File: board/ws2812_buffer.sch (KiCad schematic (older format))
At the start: 5 parts

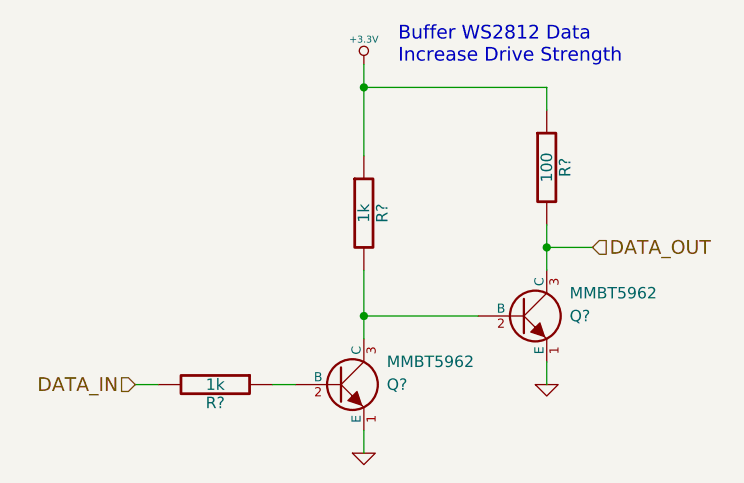
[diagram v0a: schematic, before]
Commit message: Reiner Documentation, Industrial GPIO, Driver Fix
I added documentation for the meaning of Reiner's board pins. I have
finished implemented the industrial inputs on the schematic and partial
industrial outputs. I have added some capacitors to the motor drivers.
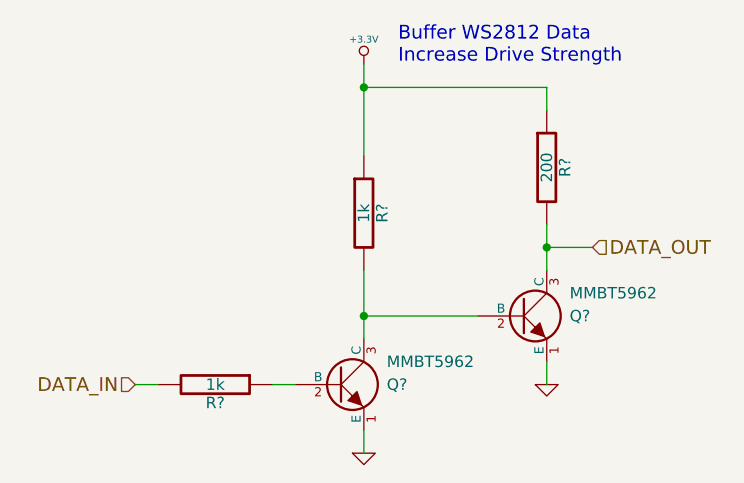
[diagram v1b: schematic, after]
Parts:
- R?: value 100 -> 200
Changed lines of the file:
@@
 $Descr USLetter 11000 8500
 encoding utf-8
-Sheet 8 10
+Sheet 8 26
 Title "WS2812 Buffered Output"
 Date ""
@@
 P 6150 4000
 F 0 "R?" V 6230 4000 50  0000 C CNN
-F 1 "100" V 6150 4000 50  0000 C CNN
+F 1 "200" V 6150 4000 50  0000 C CNN
 F 2 "" H 6150 4000 60  0000 C CNN
 F 3 "" H 6150 4000 60  0000 C CNN

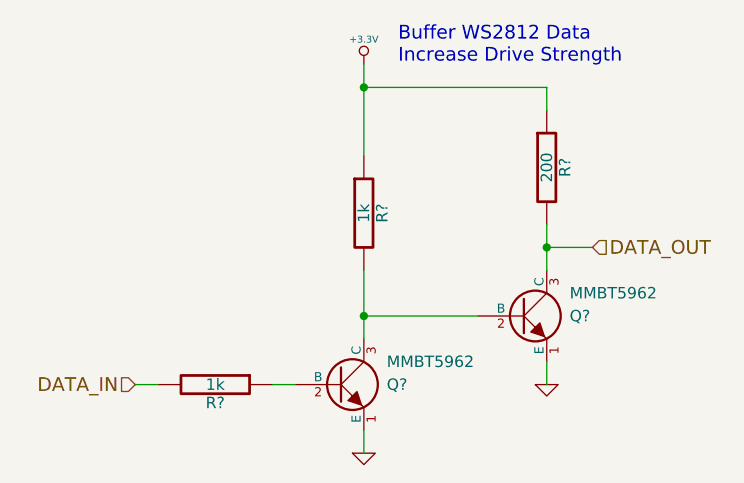
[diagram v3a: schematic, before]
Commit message: Fixed ERC Errors. Annotated all components.
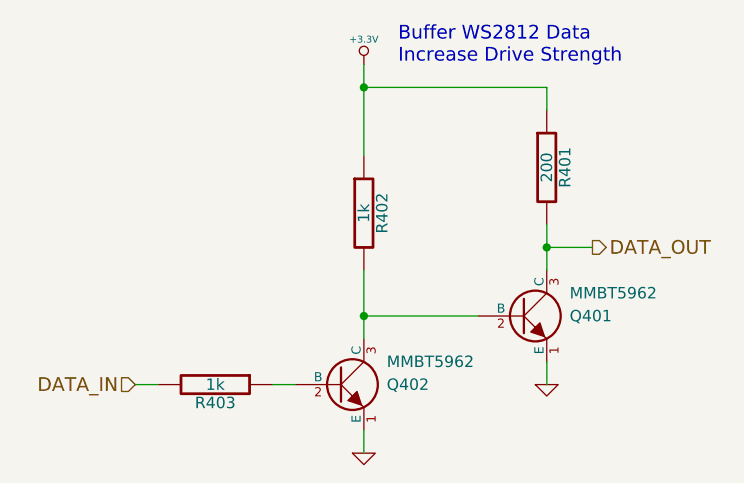
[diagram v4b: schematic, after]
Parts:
- gave numbers to parts that had none: 5
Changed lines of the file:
@@
 $EndDescr
 $Comp
-L NPN Q?
+L NPN Q402
 U 1 1 52EEEE15
 P 5250 4950
-F 0 "Q?" H 5450 4950 50  0000 L CNN
+AR Path="/52EF032B/52EEEE15" Ref="Q402"  Part="1"
+AR Path="/52EF6BF1/52EEEE15" Ref="Q502"  Part="1"
+F 0 "Q402" H 5450 4950 50  0000 L CNN
 F 1 "MMBT5962" H 5450 5050 50  0000 L CNN
 F 2 "" H 5250 4950 60  0000 C CNN
@@
 $EndComp
 $Comp
-L R R?
+L R R403
 U 1 1 52EEEE2E
 P 4700 4950
-F 0 "R?" V 4780 4950 50  0000 C CNN
+AR Path="/52EF032B/52EEEE2E" Ref="R403"  Part="1"
+AR Path="/52EF6BF1/52EEEE2E" Ref="R503"  Part="1"
+F 0 "R403" V 4780 4950 50  0000 C CNN
 F 1 "1k" V 4700 4950 50  0000 C CNN
 F 2 "" H 4700 4950 60  0000 C CNN
@@
 $EndComp
 $Comp
-L GND #PWR?
+L GND #PWR0124
 U 1 1 52EEEE49
 P 5350 5250
-F 0 "#PWR?" H 5350 5250 30  0001 C CNN
+AR Path="/52EF032B/52EEEE49" Ref="#PWR0124"  Part="1"
+AR Path="/52EF6BF1/52EEEE49" Ref="#PWR0127"  Part="1"
+F 0 "#PWR0127" H 5350 5250 30  0001 C CNN
 F 1 "GND" H 5350 5180 30  0001 C CNN
 F 2 "" H 5350 5250 60  0000 C CNN
@@
 $EndComp
 $Comp
-L R R?
+L R R402
 U 1 1 52EEEE6D
 P 5350 4200
-F 0 "R?" V 5430 4200 50  0000 C CNN
+AR Path="/52EF032B/52EEEE6D" Ref="R402"  Part="1"
+AR Path="/52EF6BF1/52EEEE6D" Ref="R502"  Part="1"
+F 0 "R402" V 5430 4200 50  0000 C CNN
 F 1 "1k" V 5350 4200 50  0000 C CNN
 F 2 "" H 5350 4200 60  0000 C CNN
@@
 $EndComp
 $Comp
-L +3.3V #PWR?
+L +3.3V #PWR0125
 U 1 1 52EEEE7E
 P 5350 3550
-F 0 "#PWR?" H 5350 3510 30  0001 C CNN
+AR Path="/52EF032B/52EEEE7E" Ref="#PWR0125"  Part="1"
+AR Path="/52EF6BF1/52EEEE7E" Ref="#PWR0128"  Part="1"
+F 0 "#PWR0128" H 5350 3510 30  0001 C CNN
 F 1 "+3.3V" H 5350 3660 30  0000 C CNN
 F 2 "" H 5350 3550 60  0000 C CNN
@@
 $EndComp
 $Comp
-L NPN Q?
+L NPN Q401
 U 1 1 52EEEE90
 P 6050 4650
-F 0 "Q?" H 6250 4650 50  0000 L CNN
+AR Path="/52EF032B/52EEEE90" Ref="Q401"  Part="1"
+AR Path="/52EF6BF1/52EEEE90" Ref="Q501"  Part="1"
+F 0 "Q401" H 6250 4650 50  0000 L CNN
 F 1 "MMBT5962" H 6250 4750 50  0000 L CNN
 F 2 "" H 6050 4650 60  0000 C CNN
@@
 $EndComp
 $Comp
-L GND #PWR?
+L GND #PWR0126
 U 1 1 52EEEE97
 P 6150 4950
-F 0 "#PWR?" H 6150 4950 30  0001 C CNN
+AR Path="/52EF032B/52EEEE97" Ref="#PWR0126"  Part="1"
+AR Path="/52EF6BF1/52EEEE97" Ref="#PWR0129"  Part="1"
+F 0 "#PWR0129" H 6150 4950 30  0001 C CNN
 F 1 "GND" H 6150 4880 30  0001 C CNN
 F 2 "" H 6150 4950 60  0000 C CNN
@@
 $EndComp
 $Comp
-L R R?
+L R R401
 U 1 1 52EEEE9E
 P 6150 4000
-F 0 "R?" V 6230 4000 50  0000 C CNN
+AR Path="/52EF032B/52EEEE9E" Ref="R401"  Part="1"
+AR Path="/52EF6BF1/52EEEE9E" Ref="R501"  Part="1"
+F 0 "R401" V 6230 4000 50  0000 C CNN
 F 1 "200" V 6150 4000 50  0000 C CNN
 F 2 "" H 6150 4000 60  0000 C CNN
@@
 Text HLabel 4350 4950 0    60   Input ~ 0
 DATA_IN
-Text HLabel 6350 4350 2    60   Input ~ 0
+Text HLabel 6350 4350 2    60   Output ~ 0
 DATA_OUT
 Wire Wire Line

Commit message: Selected Part Numbers for all Components
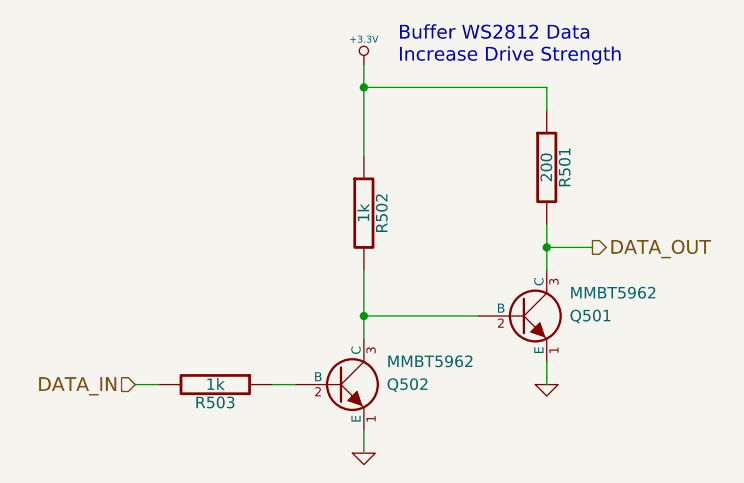
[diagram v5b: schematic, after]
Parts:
- Q401, Q402: Part Number (none) -> MMBT5962
- R401: Part Number (none) -> RC1608J201CS
- R402, R403: Part Number (none) -> RC1608J102CS
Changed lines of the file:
@@
 AR Path="/52EF032B/52EEEE15" Ref="Q402"  Part="1"
 AR Path="/52EF6BF1/52EEEE15" Ref="Q502"  Part="1"
-F 0 "Q402" H 5450 4950 50  0000 L CNN
+F 0 "Q502" H 5450 4950 50  0000 L CNN
 F 1 "MMBT5962" H 5450 5050 50  0000 L CNN
 F 2 "" H 5250 4950 60  0000 C CNN
 F 3 "" H 5250 4950 60  0000 C CNN
+F 4 "MMBT5962" H 5250 4950 60  0001 C CNN "Part Number"
 	1    5250 4950
 	1    0    0    -1
@@
 AR Path="/52EF032B/52EEEE2E" Ref="R403"  Part="1"
 AR Path="/52EF6BF1/52EEEE2E" Ref="R503"  Part="1"
-F 0 "R403" V 4780 4950 50  0000 C CNN
+F 0 "R503" V 4780 4950 50  0000 C CNN
 F 1 "1k" V 4700 4950 50  0000 C CNN
 F 2 "" H 4700 4950 60  0000 C CNN
 F 3 "" H 4700 4950 60  0000 C CNN
+F 4 "RC1608J102CS" V 4700 4950 60  0001 C CNN "Part Number"
 	1    4700 4950
 	0    1    1    0
 $EndComp
 $Comp
-L GND #PWR0124
+L GND #PWR0129
 U 1 1 52EEEE49
 P 5350 5250
-AR Path="/52EF032B/52EEEE49" Ref="#PWR0124"  Part="1"
-AR Path="/52EF6BF1/52EEEE49" Ref="#PWR0127"  Part="1"
-F 0 "#PWR0127" H 5350 5250 30  0001 C CNN
+AR Path="/52EF032B/52EEEE49" Ref="#PWR0129"  Part="1"
+AR Path="/52EF6BF1/52EEEE49" Ref="#PWR0132"  Part="1"
+F 0 "#PWR0132" H 5350 5250 30  0001 C CNN
 F 1 "GND" H 5350 5180 30  0001 C CNN
 F 2 "" H 5350 5250 60  0000 C CNN
@@
 AR Path="/52EF032B/52EEEE6D" Ref="R402"  Part="1"
 AR Path="/52EF6BF1/52EEEE6D" Ref="R502"  Part="1"
-F 0 "R402" V 5430 4200 50  0000 C CNN
+F 0 "R502" V 5430 4200 50  0000 C CNN
 F 1 "1k" V 5350 4200 50  0000 C CNN
 F 2 "" H 5350 4200 60  0000 C CNN
 F 3 "" H 5350 4200 60  0000 C CNN
+F 4 "RC1608J102CS" V 5350 4200 60  0001 C CNN "Part Number"
 	1    5350 4200
 	1    0    0    -1
 $EndComp
 $Comp
-L +3.3V #PWR0125
+L +3.3V #PWR0130
 U 1 1 52EEEE7E
 P 5350 3550
-AR Path="/52EF032B/52EEEE7E" Ref="#PWR0125"  Part="1"
-AR Path="/52EF6BF1/52EEEE7E" Ref="#PWR0128"  Part="1"
-F 0 "#PWR0128" H 5350 3510 30  0001 C CNN
+AR Path="/52EF032B/52EEEE7E" Ref="#PWR0130"  Part="1"
+AR Path="/52EF6BF1/52EEEE7E" Ref="#PWR0133"  Part="1"
+F 0 "#PWR0133" H 5350 3510 30  0001 C CNN
 F 1 "+3.3V" H 5350 3660 30  0000 C CNN
 F 2 "" H 5350 3550 60  0000 C CNN
@@
 AR Path="/52EF032B/52EEEE90" Ref="Q401"  Part="1"
 AR Path="/52EF6BF1/52EEEE90" Ref="Q501"  Part="1"
-F 0 "Q401" H 6250 4650 50  0000 L CNN
+F 0 "Q501" H 6250 4650 50  0000 L CNN
 F 1 "MMBT5962" H 6250 4750 50  0000 L CNN
 F 2 "" H 6050 4650 60  0000 C CNN
 F 3 "" H 6050 4650 60  0000 C CNN
+F 4 "MMBT5962" H 6050 4650 60  0001 C CNN "Part Number"
 	1    6050 4650
 	1    0    0    -1
 $EndComp
 $Comp
-L GND #PWR0126
+L GND #PWR0131
 U 1 1 52EEEE97
 P 6150 4950
-AR Path="/52EF032B/52EEEE97" Ref="#PWR0126"  Part="1"
-AR Path="/52EF6BF1/52EEEE97" Ref="#PWR0129"  Part="1"
-F 0 "#PWR0129" H 6150 4950 30  0001 C CNN
+AR Path="/52EF032B/52EEEE97" Ref="#PWR0131"  Part="1"
+AR Path="/52EF6BF1/52EEEE97" Ref="#PWR0134"  Part="1"
+F 0 "#PWR0134" H 6150 4950 30  0001 C CNN
 F 1 "GND" H 6150 4880 30  0001 C CNN
 F 2 "" H 6150 4950 60  0000 C CNN
@@
 AR Path="/52EF032B/52EEEE9E" Ref="R401"  Part="1"
 AR Path="/52EF6BF1/52EEEE9E" Ref="R501"  Part="1"
-F 0 "R401" V 6230 4000 50  0000 C CNN
+F 0 "R501" V 6230 4000 50  0000 C CNN
 F 1 "200" V 6150 4000 50  0000 C CNN
 F 2 "" H 6150 4000 60  0000 C CNN
 F 3 "" H 6150 4000 60  0000 C CNN
+F 4 "RC1608J201CS" V 6150 4000 60  0001 C CNN "Part Number"
 	1    6150 4000
 	1    0    0    -1

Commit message: Digikey Number + Link
Added a digikey part number and link to all components.
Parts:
- Q401, Q402: Digikey Number (none) -> MMBT5962CT-ND; Part Number MMBT5962 -> (none)
- R401: Digikey Number (none) -> 1276-5045-1-ND; Part Number RC1608J201CS -> (none)
- R402, R403: Digikey Number (none) -> 1276-5062-1-ND; Part Number RC1608J102CS -> (none)
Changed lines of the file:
@@
 F 1 "MMBT5962" H 5450 5050 50  0000 L CNN
 F 2 "" H 5250 4950 60  0000 C CNN
-F 3 "" H 5250 4950 60  0000 C CNN
-F 4 "MMBT5962" H 5250 4950 60  0001 C CNN "Part Number"
+F 3 "http://www.digikey.ca/product-detail/en/MMBT5962/MMBT5962CT-ND/4213632" H 5250 4950 60  0001 C CNN
+F 4 "MMBT5962CT-ND" H 6900 4550 60  0001 C CNN "Digikey Number"
 	1    5250 4950
 	1    0    0    -1
@@
 F 1 "1k" V 4700 4950 50  0000 C CNN
 F 2 "" H 4700 4950 60  0000 C CNN
-F 3 "" H 4700 4950 60  0000 C CNN
-F 4 "RC1608J102CS" V 4700 4950 60  0001 C CNN "Part Number"
+F 3 "http://www.digikey.ca/product-detail/en/RC1608J102CS/1276-5062-1-ND/3968034" H 4700 4950 60  0001 C CNN
+F 4 "1276-5062-1-ND" H 6900 4550 60  0001 C CNN "Digikey Number"
 	1    4700 4950
 	0    1    1    0
@@
 F 1 "1k" V 5350 4200 50  0000 C CNN
 F 2 "" H 5350 4200 60  0000 C CNN
-F 3 "" H 5350 4200 60  0000 C CNN
-F 4 "RC1608J102CS" V 5350 4200 60  0001 C CNN "Part Number"
+F 3 "http://www.digikey.ca/product-detail/en/RC1608J102CS/1276-5062-1-ND/3968034" H 5350 4200 60  0001 C CNN
+F 4 "1276-5062-1-ND" H 6900 4550 60  0001 C CNN "Digikey Number"
 	1    5350 4200
 	1    0    0    -1
@@
 F 1 "MMBT5962" H 6250 4750 50  0000 L CNN
 F 2 "" H 6050 4650 60  0000 C CNN
-F 3 "" H 6050 4650 60  0000 C CNN
-F 4 "MMBT5962" H 6050 4650 60  0001 C CNN "Part Number"
+F 3 "http://www.digikey.ca/product-detail/en/MMBT5962/MMBT5962CT-ND/4213632" H 6050 4650 60  0001 C CNN
+F 4 "MMBT5962CT-ND" H 6900 4550 60  0001 C CNN "Digikey Number"
 	1    6050 4650
 	1    0    0    -1
@@
 F 1 "200" V 6150 4000 50  0000 C CNN
 F 2 "" H 6150 4000 60  0000 C CNN
-F 3 "" H 6150 4000 60  0000 C CNN
-F 4 "RC1608J201CS" V 6150 4000 60  0001 C CNN "Part Number"
+F 3 "http://www.digikey.ca/product-detail/en/RC1608J201CS/1276-5045-1-ND/3968017" H 6150 4000 60  0001 C CNN
+F 4 "1276-5045-1-ND" H 6900 4550 60  0001 C CNN "Digikey Number"
 	1    6150 4000
 	1    0    0    -1
